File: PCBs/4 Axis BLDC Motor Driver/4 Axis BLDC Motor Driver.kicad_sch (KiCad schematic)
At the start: 1 part, among them U1 ESP32-S3-WROOM-1

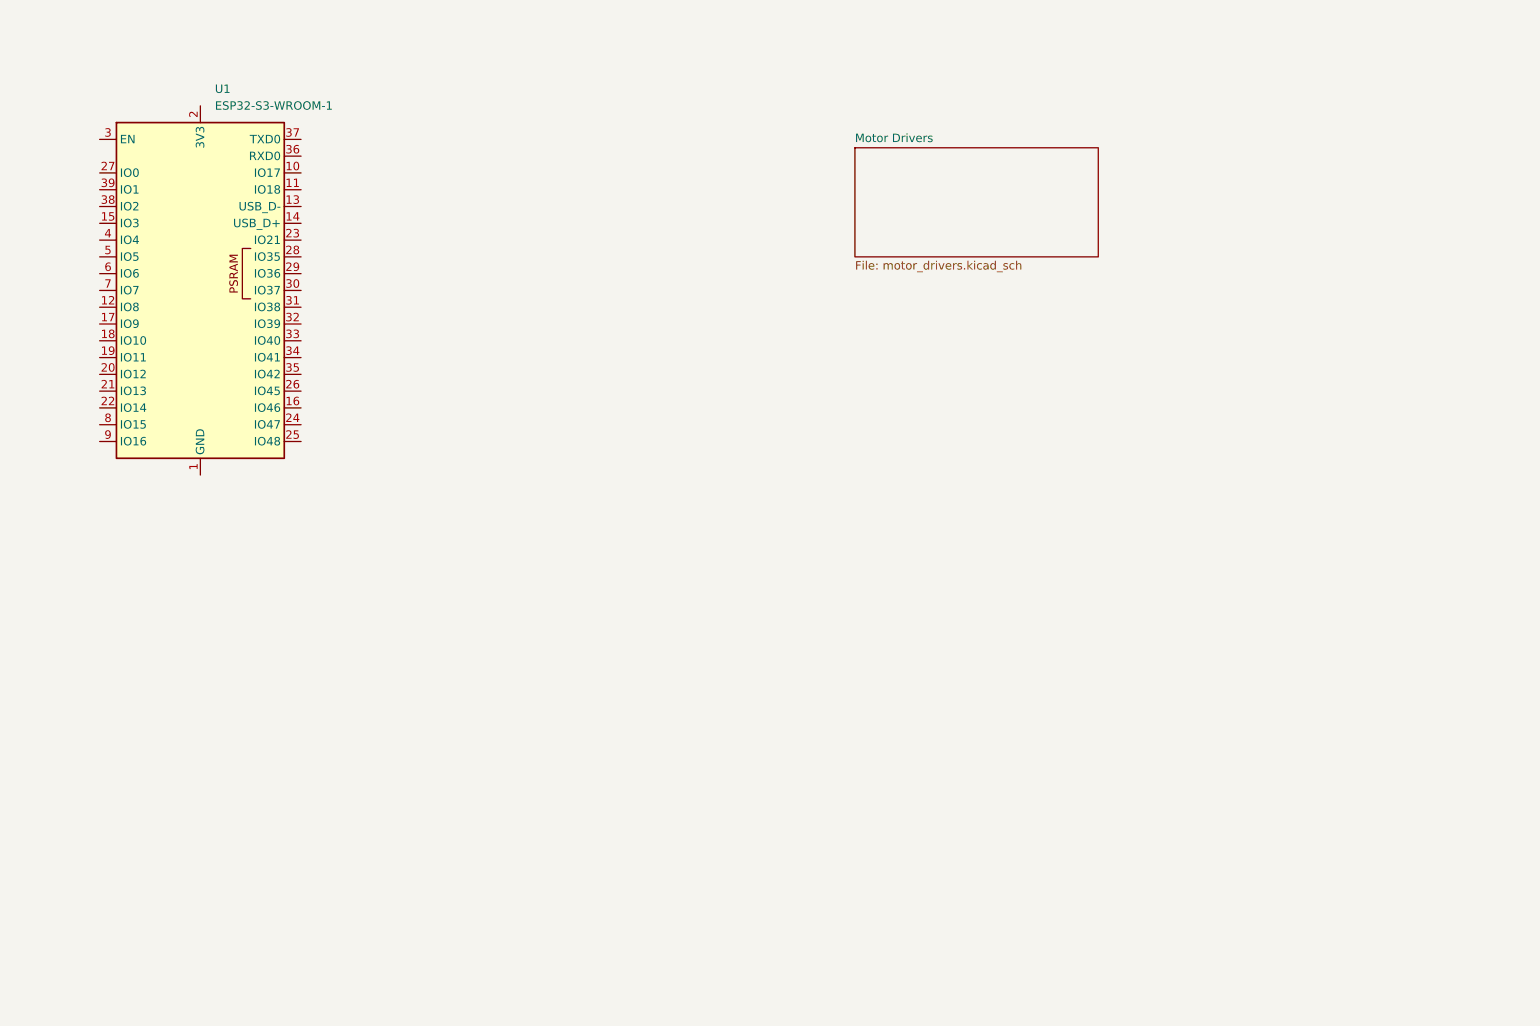
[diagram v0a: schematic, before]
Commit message: Finish DRV8301 symbol, start implementing circuitry around it
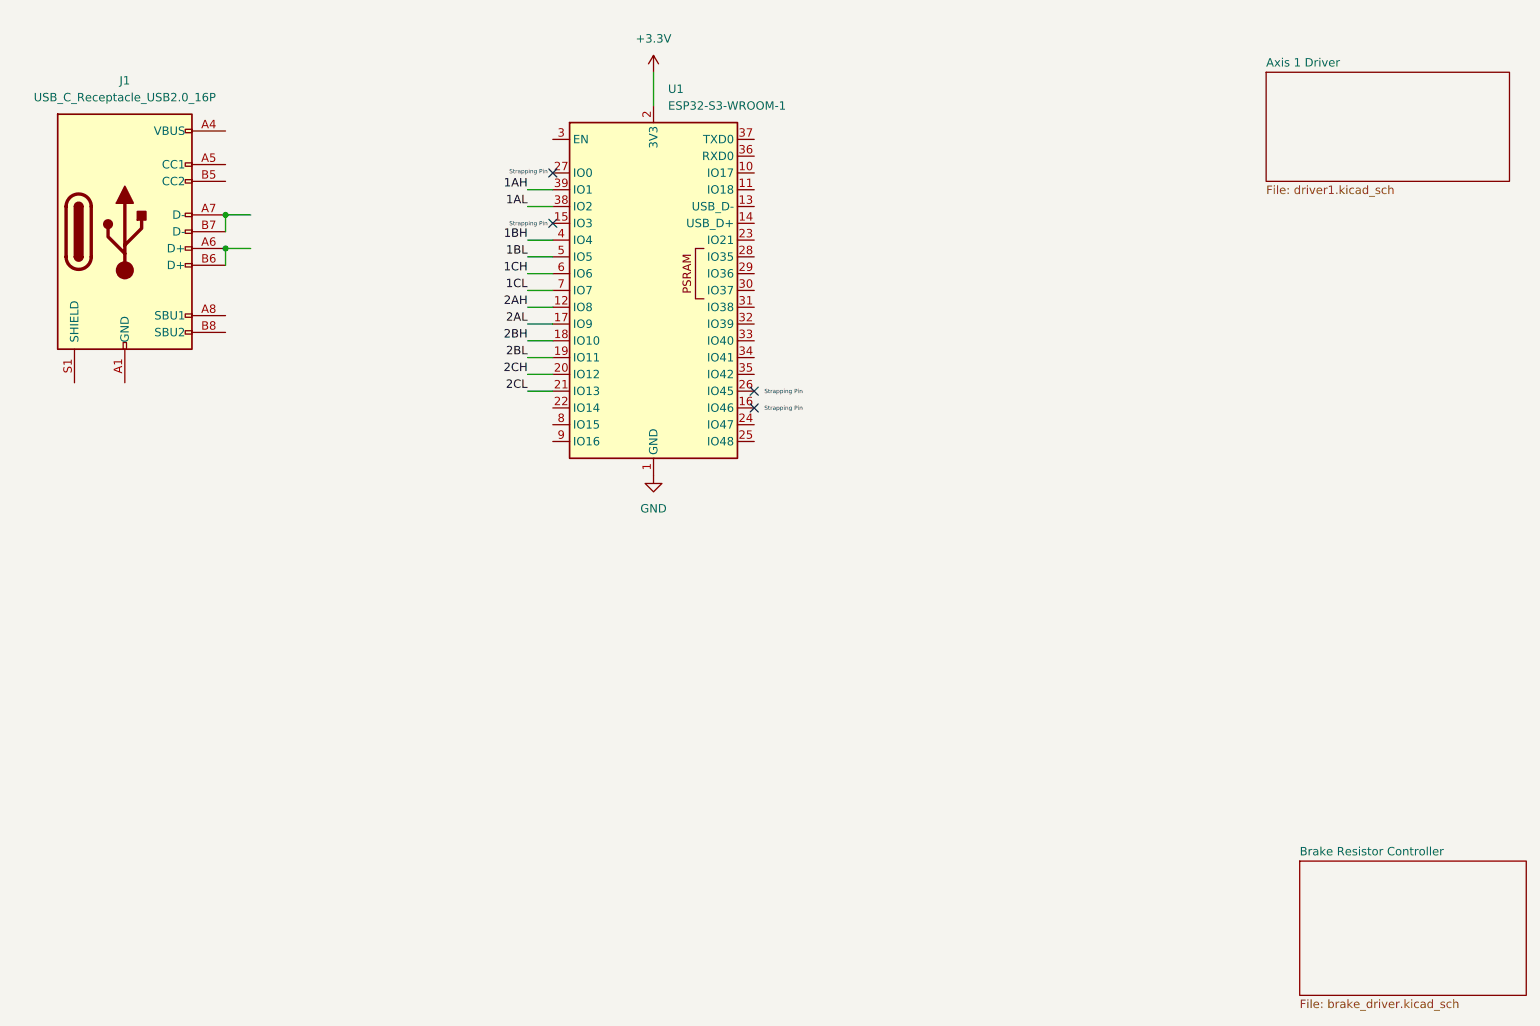
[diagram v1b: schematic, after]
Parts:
- added J1: USB_C_Receptacle_USB2.0_16P, symbol Connector:USB_C_Receptacle_USB2.0_16P
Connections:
- net GND: now reaches U1.1 (GND), U1.40 (GND), U1.41 (GND)
- net 2AH: now reaches U1.12 (IO8)
- net 2AL: now reaches U1.17 (IO9)
- net 2BH: now reaches U1.18 (IO10)
- net 2BL: now reaches U1.19 (IO11)
- net +3.3V: now reaches U1.2 (3V3)
- net 2CH: now reaches U1.20 (IO12)
- net 2CL: now reaches U1.21 (IO13)
- net 1AL: now reaches U1.38 (IO2)
- net 1AH: now reaches U1.39 (IO1)
- net 1BH: now reaches U1.4 (IO4)
- net 1BL: now reaches U1.5 (IO5)
- net 1CH: now reaches U1.6 (IO6)
- net 1CL: now reaches U1.7 (IO7)
- new net: J1.A1 (GND), J1.A12 (GND), J1.B1 (GND), J1.B12 (GND)
- new net: J1.A4 (VBUS), J1.A9 (VBUS), J1.B4 (VBUS), J1.B9 (VBUS)
- new net: J1.A6 (D+), J1.B6 (D+)
- new net: J1.A7 (D-), J1.B7 (D-)
- no-connect marks 0 -> 4
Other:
- sheet Motor Drivers renamed Axis 1 Driver
- added sheet Brake Resistor Controller (brake_driver.kicad_sch)
- sheet Axis 1 Driver: file motor_drivers.kicad_sch -> driver1.kicad_sch
- note added: "Strapping Pin"

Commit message: Add AMS1117 LDO to give 3.3V power to MCU
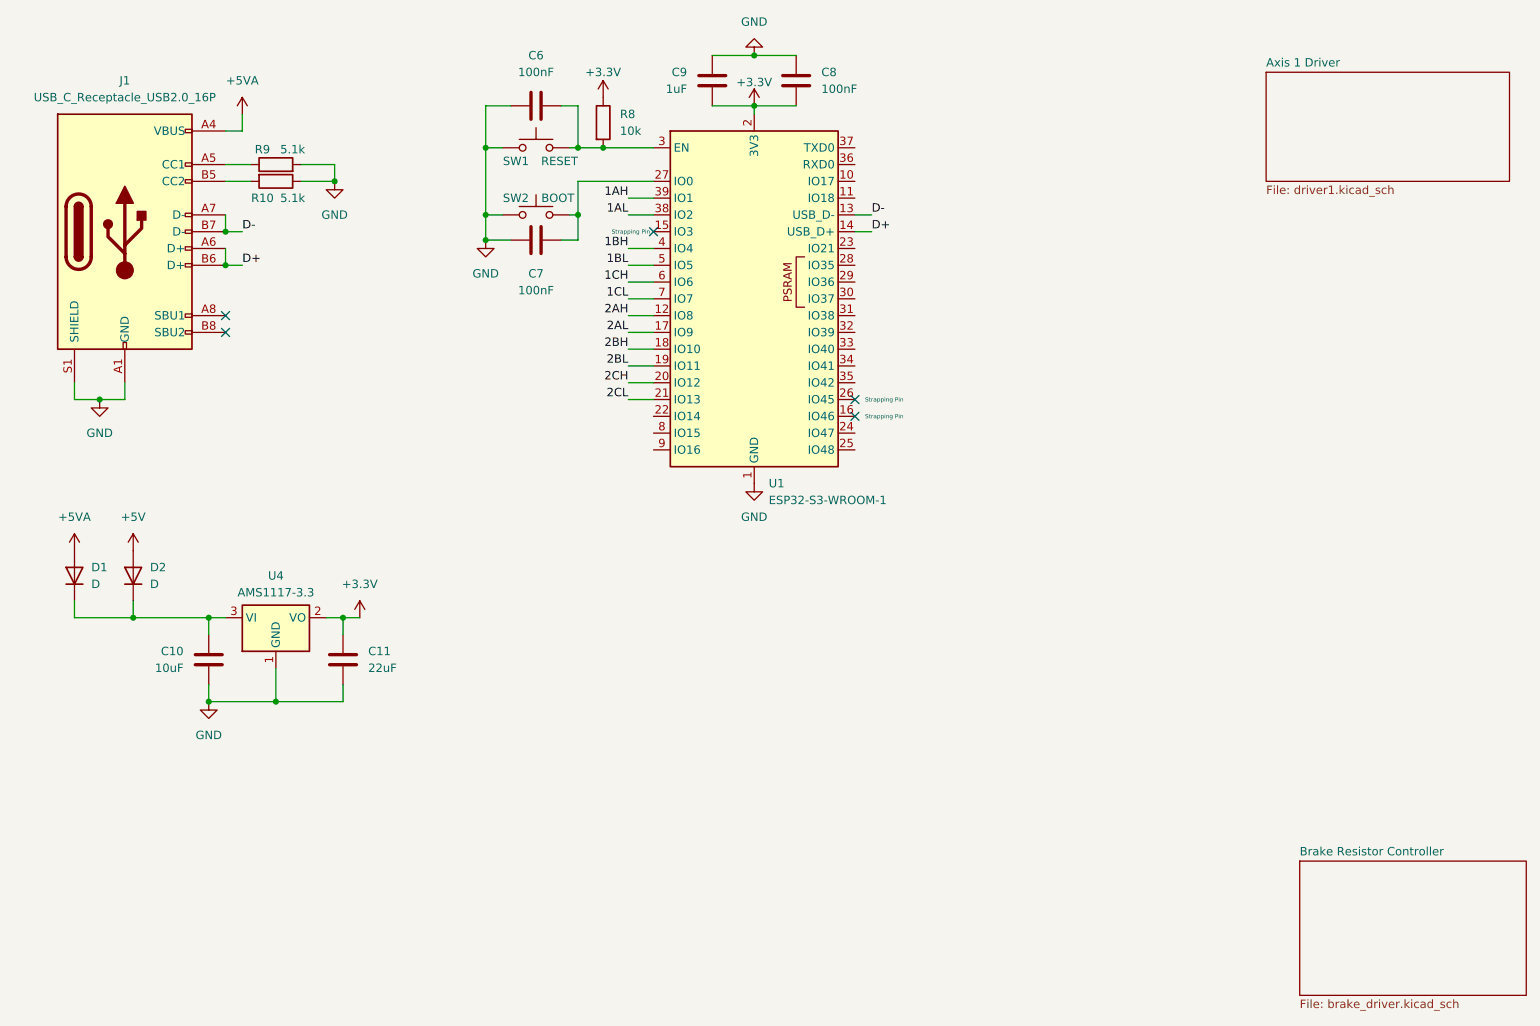
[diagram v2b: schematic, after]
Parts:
- added C10: 10uF, symbol Device:C
- added C11: 22uF, symbol Device:C
- added C6, C7, C8: 100nF, symbol Device:C
- added C9: 1uF, symbol Device:C
- added D1, D2: D, symbol Device:D
- added R10, R9: 5.1k, symbol Device:R
- added R8: 10k, symbol Device:R
- added SW1: RESET, symbol Switch:SW_Push
- added SW2: BOOT, symbol Switch:SW_Push
- added U4: AMS1117-3.3, Package_TO_SOT_SMD:SOT-223-3_TabPin2, symbol Regulator_Linear:AMS1117-3.3
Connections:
- net +3.3V: now also C11.1, C8.1, C9.1, R8.1, U4.2 (VO)
- net GND: now also J1.A1 (GND), J1.A12 (GND), J1.B1 (GND), J1.B12 (GND), J1.S1 (SHIELD), C10.2, C11.2, C6.1, C7.2, C8.2, C9.2, R10.1, R9.2, SW1.1, SW2.1, U4.1 (GND)
- net +5VA: now reaches J1.A4 (VBUS), J1.A9 (VBUS), J1.B4 (VBUS), J1.B9 (VBUS)
- net +5VA: now also D1.2 (A)
- net at J1.A5 (CC1): now also R9.1
- net D+: now reaches J1.A6 (D+), J1.B6 (D+)
- net D+: now also U1.14 (USB_D+)
- net D-: now reaches J1.A7 (D-), J1.B7 (D-)
- net D-: now also U1.13 (USB_D-)
- net at J1.B5 (CC2): now also R10.2
- net at U1.27 (IO0): now also C7.1, SW2.2
- net at U1.3 (EN): now also C6.2, R8.2, SW1.2
- new net: C10.1, D1.1 (K), D2.1 (K), U4.3 (VI)
- new net +5V: D2.2 (A)
- no-connect marks 4 -> 5
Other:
- moved on the sheet: U1
